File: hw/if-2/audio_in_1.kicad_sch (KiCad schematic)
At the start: 0 parts

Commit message: First draft of schematic
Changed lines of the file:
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@@
 	(text "(Will Be Copy of R0 Audio Input)"
 		(exclude_from_sim no)
-		(at 149.86 92.964 0)
+		(at 140.462 101.6 0)
 		(effects
 			(font

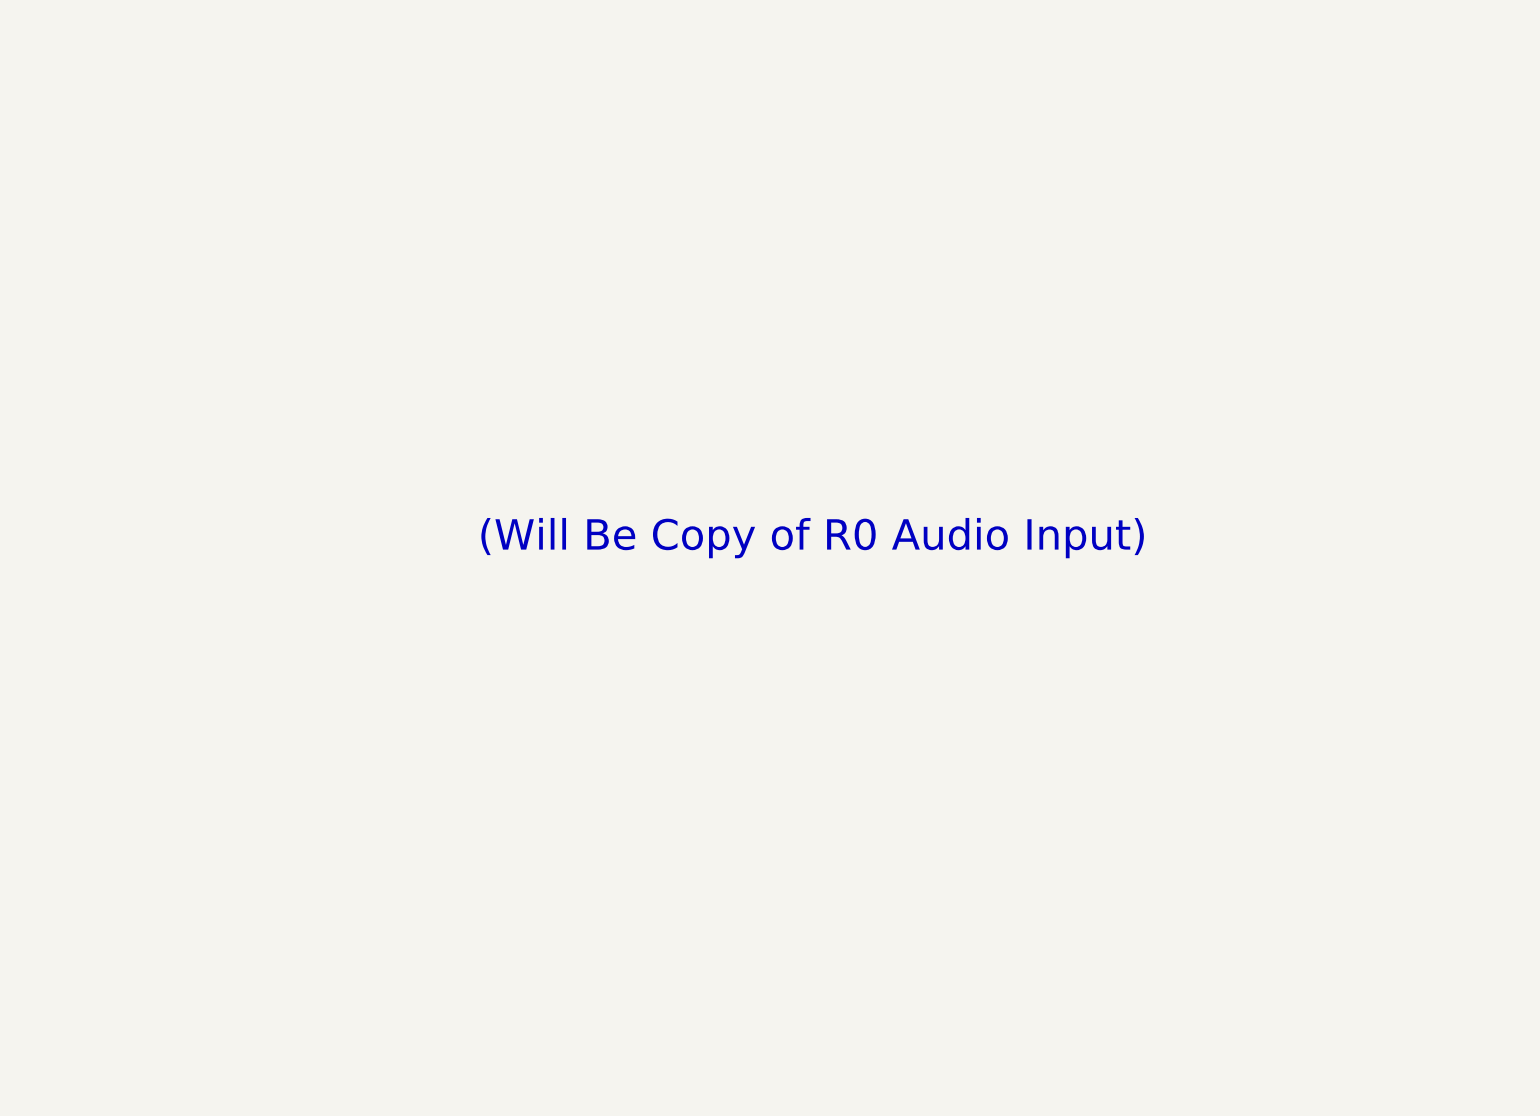
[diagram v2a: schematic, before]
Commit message: Ready to do layout on IF2 board
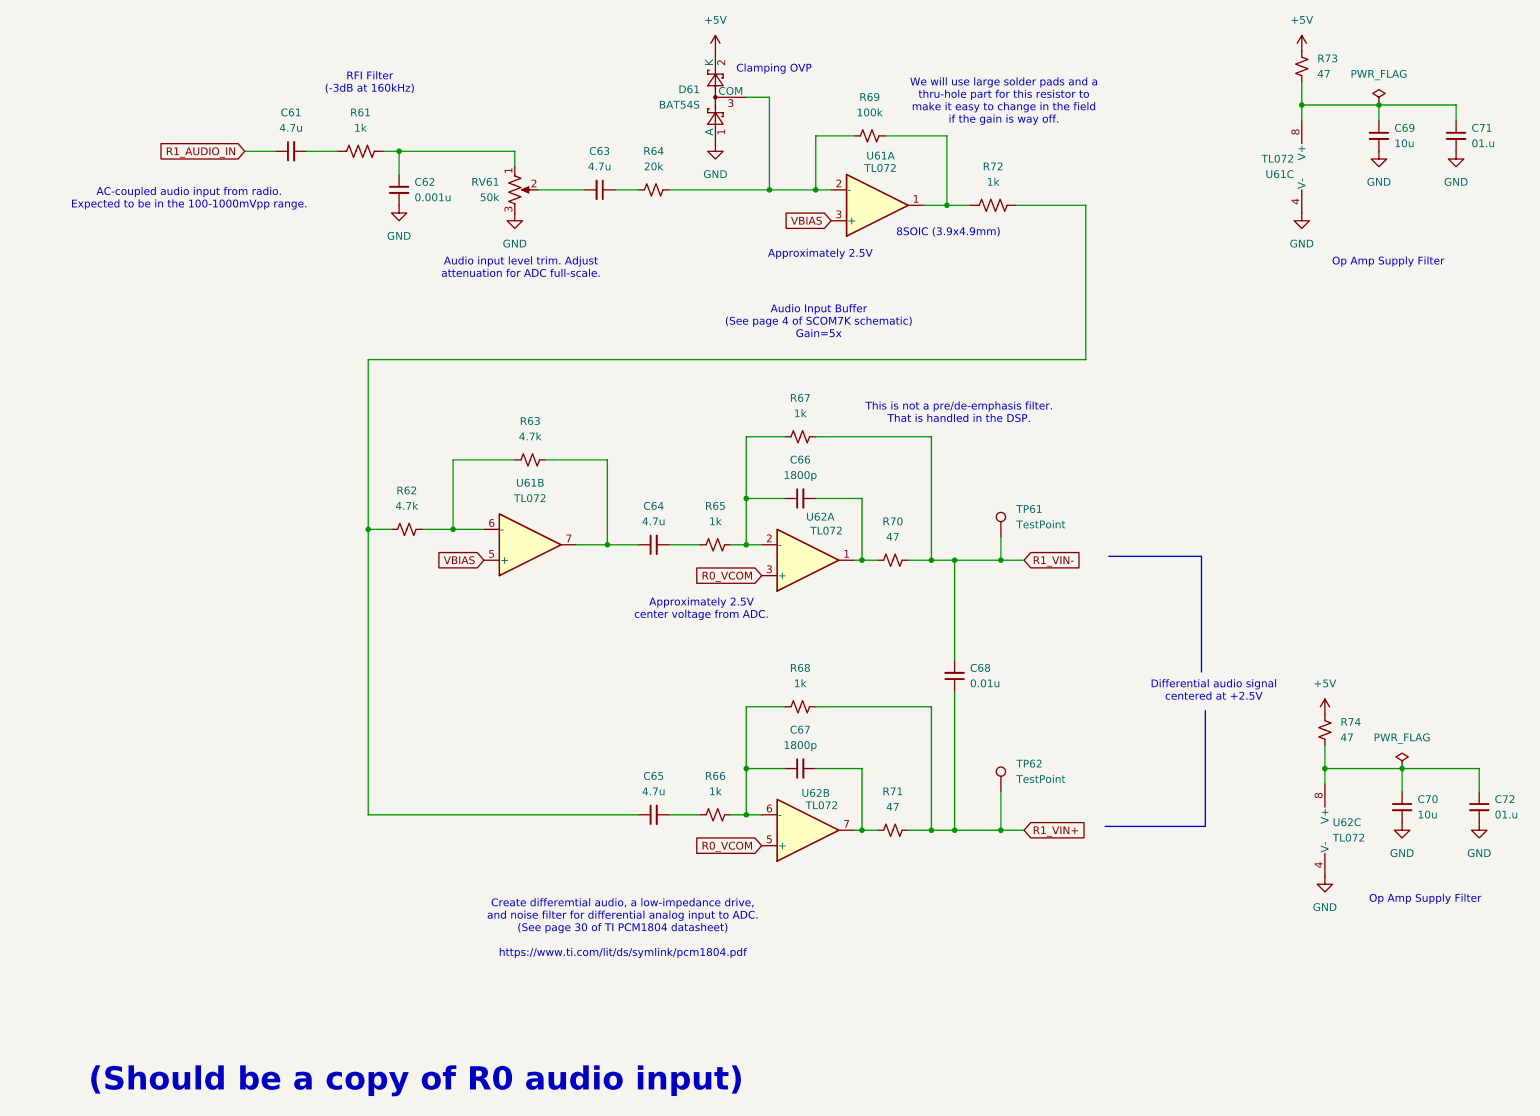
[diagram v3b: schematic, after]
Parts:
- added C61, C63, C64, C65: 4.7u, Capacitor_SMD:C_0805_2012Metric_Pad1.18x1.45mm_HandSolder, symbol Device:C_Small
- added C62: 0.001u, Capacitor_SMD:C_0805_2012Metric_Pad1.18x1.45mm_HandSolder, symbol Device:C_Small
- added C66, C67: 1800p, Capacitor_SMD:C_0805_2012Metric_Pad1.18x1.45mm_HandSolder, symbol Device:C_Small
- added C68: 0.01u, Capacitor_SMD:C_0805_2012Metric_Pad1.18x1.45mm_HandSolder, symbol Device:C_Small
- added C69, C70: 10u, Capacitor_SMD:C_0805_2012Metric_Pad1.18x1.45mm_HandSolder, symbol Device:C_Small
- added C71, C72: 01.u, Capacitor_SMD:C_0805_2012Metric_Pad1.18x1.45mm_HandSolder, symbol Device:C_Small
- added D61: BAT54S, Package_TO_SOT_SMD:SOT-23, symbol Diode:BAT54S
- added R61, R72: 1k, Resistor_SMD:R_0805_2012Metric_Pad1.20x1.40mm_HandSolder, symbol Device:R_US
- added R62, R63: 4.7k, Resistor_SMD:R_0805_2012Metric_Pad1.20x1.40mm_HandSolder, symbol Device:R_Small_US
- added R64: 20k, Resistor_SMD:R_0805_2012Metric_Pad1.20x1.40mm_HandSolder, symbol Device:R_Small_US
- added R65, R66, R67, R68: 1k, Resistor_SMD:R_0805_2012Metric_Pad1.20x1.40mm_HandSolder, symbol Device:R_Small_US
- added R69: 100k, Resistor_SMD:R_0805_2012Metric_Pad1.20x1.40mm_HandSolder, symbol Device:R_Small_US
- added R70, R71, R73, R74: 47, Resistor_SMD:R_0805_2012Metric_Pad1.20x1.40mm_HandSolder, symbol Device:R_Small_US
- added RV61: 50k, bruce-footprints:POT_3362P, symbol Device:R_Potentiometer_US
- added TP61, TP62: TestPoint, TestPoint:TestPoint_Pad_2.5x2.5mm, symbol Connector:TestPoint
- added U61, U62: TL072, Package_SO:SOIC-8_3.9x4.9mm_P1.27mm, symbol Amplifier_Operational:TL072
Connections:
- new net: C64.1, R63.2, U61.7
- new net: C64.2, R65.1
- new net: C69.1, C71.1, R73.2, U61.8 (V+)
- new net: C70.1, C72.1, R74.2, U62.8 (V+)
- new net: R62.2, R63.1, U61.6 (-)
- new net: C66.1, R65.2, R67.1, U62.2 (-)
- new net: D61.3 (COM), R64.2, R69.1, U61.2 (-)
- new net: R69.2, R72.1, U61.1
- new net: C66.2, R70.1, U62.1
- new net: C67.2, R71.1, U62.7
- new net: C63.1, R64.1
- new net: C63.2, RV61.2
- new net: C61.2, R61.1
- new net: C67.1, R66.2, R68.1, U62.6 (-)
- new net: C62.1, R61.2, RV61.1
- new net: C65.1, R62.1, R72.2
- new net: C65.2, R66.1
- new net +5V: D61.2 (K), R73.1, R74.1
- new net GND: C62.2, C69.2, C70.2, C71.2, C72.2, D61.1 (A), RV61.3, U61.4 (V-), U62.4 (V-)
- new net R0_VCOM: U62.3 (+), U62.5 (+)
- new net R1_AUDIO_IN: C61.1
- new net R1_VIN+: C68.1, R68.2, R71.2, TP62.1
- new net R1_VIN-: C68.2, R67.2, R70.2, TP61.1
- new net VBIAS: U61.3 (+), U61.5 (+)
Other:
- note added: "(Should be a copy of R0 audio input)"
- note added: "8SOIC (3.9x4.9mm)"
- note added: "AC-coupled audio input from radio. Expected to be in the 100-1000mVpp range."
- note added: "Approximately 2.5V"
- note added: "Approximately 2.5V center voltage from ADC."
- note added: "Audio Input Buffer (See page 4 of SCOM7K schematic) Gain=5x"
- note added: "Audio input level trim. Adjust attenuation for ADC full-scale."
- note added: "Clamping OVP"
- note added: "Create differemtial audio, a low-impedance drive, and noise filter for differential analog input to ADC. (See page 30 of TI PCM1804 datasheet) https://www.ti.com/lit/ds/symlink/pcm1804.pdf"
- note added: "Differential audio signal centered at +2.5V"
- note added: "Op Amp Supply Filter"
- note added: "RFI Filter (-3dB at 160kHz)"
- note added: "This is not a pre/de-emphasis filter. That is handled in the DSP."
- note added: "We will use large solder pads and a thru-hole part for this resistor to make it easy to change in the field if the gain is way off."
- note removed: "(Will Be Copy of R0 Audio Input)"
- title: Audio Input Processing (Radio 1) -> COS/CTCSS/PTT Controls (Radio 1)

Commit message: Making progress on layout
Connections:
- net at R63.2, U61.7: now also C65.1; no longer C64.1
- net at R62.1, R72.2: now also C64.1; no longer C65.1
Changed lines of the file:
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@@
 	(title_block
 		(title "COS/CTCSS/PTT Controls (Radio 1)")
-		(date "2025-03-18")
+		(date "2025-05-09")
 		(rev "2")
 		(company "Bruce MacKinnon KC1FSZ")
@@
 	)
 	(junction
-		(at 67.31 100.33)
+		(at 111.76 72.39)
 		(diameter 0)
 		(color 0 0 0 0)
@@
 	)
 	(junction
+		(at 148.59 149.86)
+		(diameter 0)
+		(color 0 0 0 0)
+	)
+	(junction
+		(at 129.54 102.87)
+		(diameter 0)
+		(color 0 0 0 0)
+	)
+	(junction
+		(at 233.68 30.48)
+		(diameter 0)
+		(color 0 0 0 0)
+	)
+	(junction
+		(at 220.98 30.48)
+		(diameter 0)
+		(color 0 0 0 0)
+	)
+	(junction
+		(at 163.83 149.86)
+		(diameter 0)
+		(color 0 0 0 0)
+	)
+	(junction
+		(at 148.59 105.41)
+		(diameter 0)
+		(color 0 0 0 0)
+	)
+	(junction
 		(at 106.68 102.87)
 		(diameter 0)
@@
 	)
 	(junction
-		(at 148.59 149.86)
-		(diameter 0)
-		(color 0 0 0 0)
-	)
-	(junction
-		(at 129.54 102.87)
-		(diameter 0)
-		(color 0 0 0 0)
-	)
-	(junction
-		(at 233.68 30.48)
-		(diameter 0)
-		(color 0 0 0 0)
-	)
-	(junction
-		(at 220.98 30.48)
-		(diameter 0)
-		(color 0 0 0 0)
-	)
-	(junction
-		(at 163.83 149.86)
-		(diameter 0)
-		(color 0 0 0 0)
-	)
-	(junction
-		(at 148.59 105.41)
-		(diameter 0)
-		(color 0 0 0 0)
-	)
-	(junction
 		(at 171.45 149.86)
 		(diameter 0)
@@
 	(wire
 		(pts
+			(xy 106.68 102.87) (xy 106.68 147.32)
+		)
+		(stroke
+			(width 0)
+			(type default)
+		)
+	)
+	(wire
+		(pts
 			(xy 69.85 38.1) (xy 72.39 38.1)
 		)
@@
 	(wire
 		(pts
-			(xy 67.31 100.33) (xy 67.31 147.32)
-		)
-		(stroke
-			(width 0)
-			(type default)
-		)
-	)
-	(wire
-		(pts
 			(xy 171.45 105.41) (xy 175.26 105.41)
 		)
@@
 	(wire
 		(pts
+			(xy 111.76 72.39) (xy 111.76 102.87)
+		)
+		(stroke
+			(width 0)
+			(type default)
+		)
+	)
+	(wire
+		(pts
+			(xy 111.76 72.39) (xy 67.31 72.39)
+		)
+		(stroke
+			(width 0)
+			(type default)
+		)
+	)
+	(wire
+		(pts
 			(xy 158.75 46.99) (xy 162.56 46.99)
 		)
@@
 	(wire
 		(pts
+			(xy 106.68 147.32) (xy 111.76 147.32)
+		)
+		(stroke
+			(width 0)
+			(type default)
+		)
+	)
+	(wire
+		(pts
 			(xy 148.59 149.86) (xy 151.13 149.86)
 		)
@@
 	(wire
 		(pts
-			(xy 67.31 147.32) (xy 111.76 147.32)
-		)
-		(stroke
-			(width 0)
-			(type default)
-		)
-	)
-	(wire
-		(pts
 			(xy 67.31 100.33) (xy 71.12 100.33)
 		)
@@
 	(wire
 		(pts
-			(xy 185.42 72.39) (xy 67.31 72.39)
+			(xy 185.42 72.39) (xy 111.76 72.39)
 		)
 		(stroke
@@
 		)
 		(stroke
-			(width 0)
-			(type default)
-		)
-	)
-	(wire
-		(pts
-			(xy 106.68 102.87) (xy 111.76 102.87)
-		)
-		(stroke

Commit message: Making progress on layout
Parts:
- renumbered TP61 to TP4, TP62 to TP5
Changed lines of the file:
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@@
 		(dnp no)
 		(fields_autoplaced yes)
-		(property "Reference" "TP62"
+		(property "Reference" "TP5"
 			(at 173.99 138.9379 0)
 			(effects
@@
 			(project "if-2"
 				(path "/a8c2d6aa-29bb-49bd-a367-0d62a0a32480/bbe47db2-4e3f-4928-a954-056c7fb1570e"
-					(reference "TP62")
+					(reference "TP5")
 					(unit 1)
 				)
@@
 		(dnp no)
 		(fields_autoplaced yes)
-		(property "Reference" "TP61"
+		(property "Reference" "TP4"
 			(at 173.99 97.0279 0)
 			(effects
@@
 			(project "if-2"
 				(path "/a8c2d6aa-29bb-49bd-a367-0d62a0a32480/bbe47db2-4e3f-4928-a954-056c7fb1570e"
-					(reference "TP61")
-					(unit 1)
-				)
+					(reference "TP4")
+					(unit 1)
+				)

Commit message: Progress on layout
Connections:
- net R0_VCOM renamed R1_VCOM
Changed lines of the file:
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@@
 		)
 	)
-	(global_label "R0_VCOM"
+	(global_label "R1_VCOM"
 		(shape input)
 		(at 132.08 152.4 180)
@@
 		)
 	)
-	(global_label "R0_VCOM"
+	(global_label "R1_VCOM"
 		(shape input)
 		(at 132.08 107.95 180)
